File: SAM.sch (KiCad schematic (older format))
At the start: 25 parts

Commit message: ...and now the schematics are in git
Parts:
- removed U?: SAMD21G17A-MU, tm-kicad-lib:QFN-48-1EP-7mm, symbol SAMD21G14A-MU
- added C?: 100nF, tm-kicad-lib:SMD-0402-C, symbol TM_C
- added U?: ATSAMD21J18A-MUT, QFN64, symbol ATSAMD21J18A-MUT
- C?: value 100nF -> 1uF
- J?: value CONN_02X05 DNP -> CONN_02x05, 0.05\"
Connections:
- net labels added: UUT_SWCLK, UUT_SWDIO
- wire segments 144 -> 149
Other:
- moved on the sheet: C?, L?, R?, TP?, X?

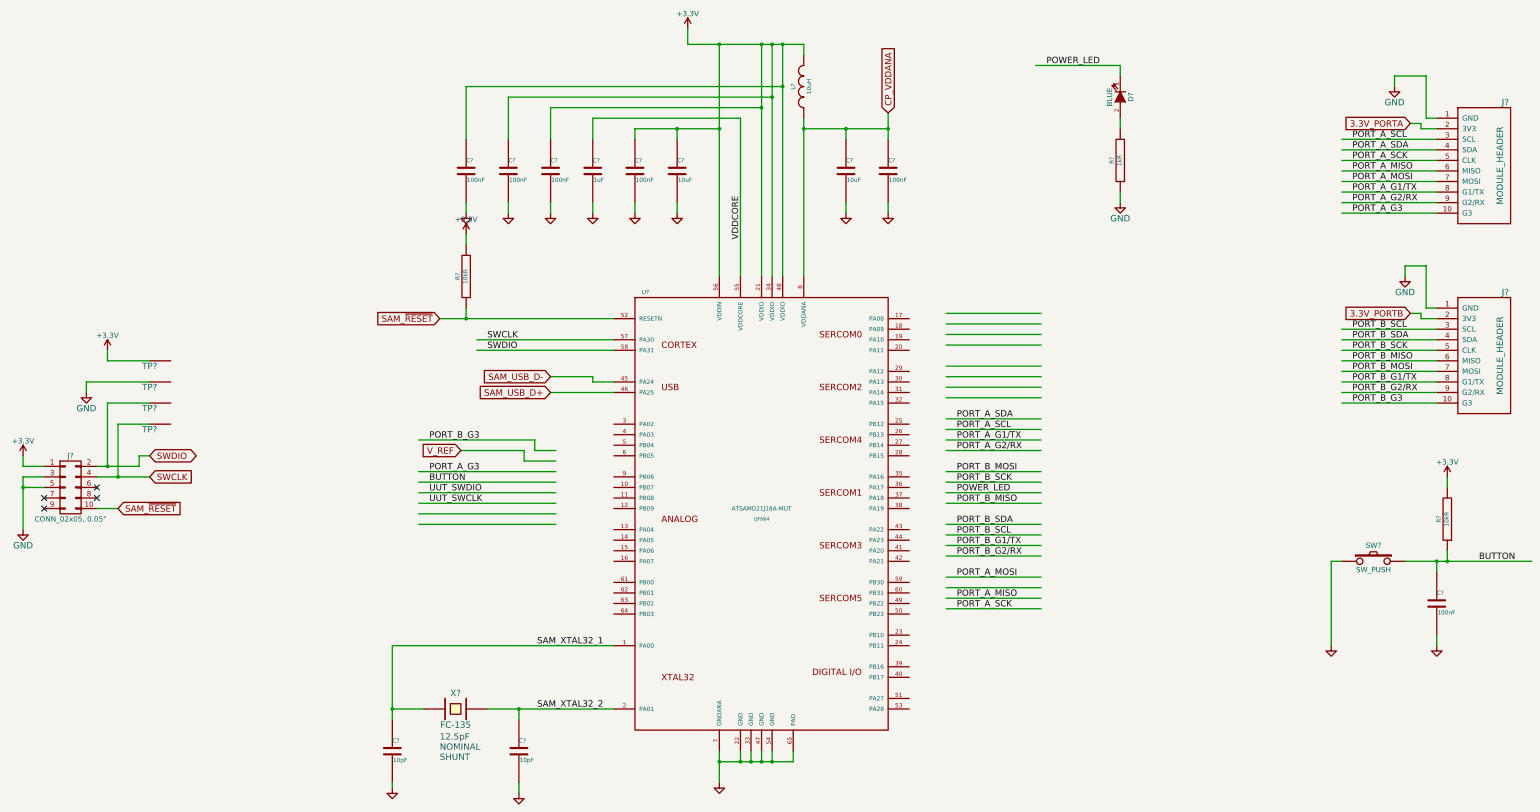
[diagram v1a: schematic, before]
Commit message: sercoms in place
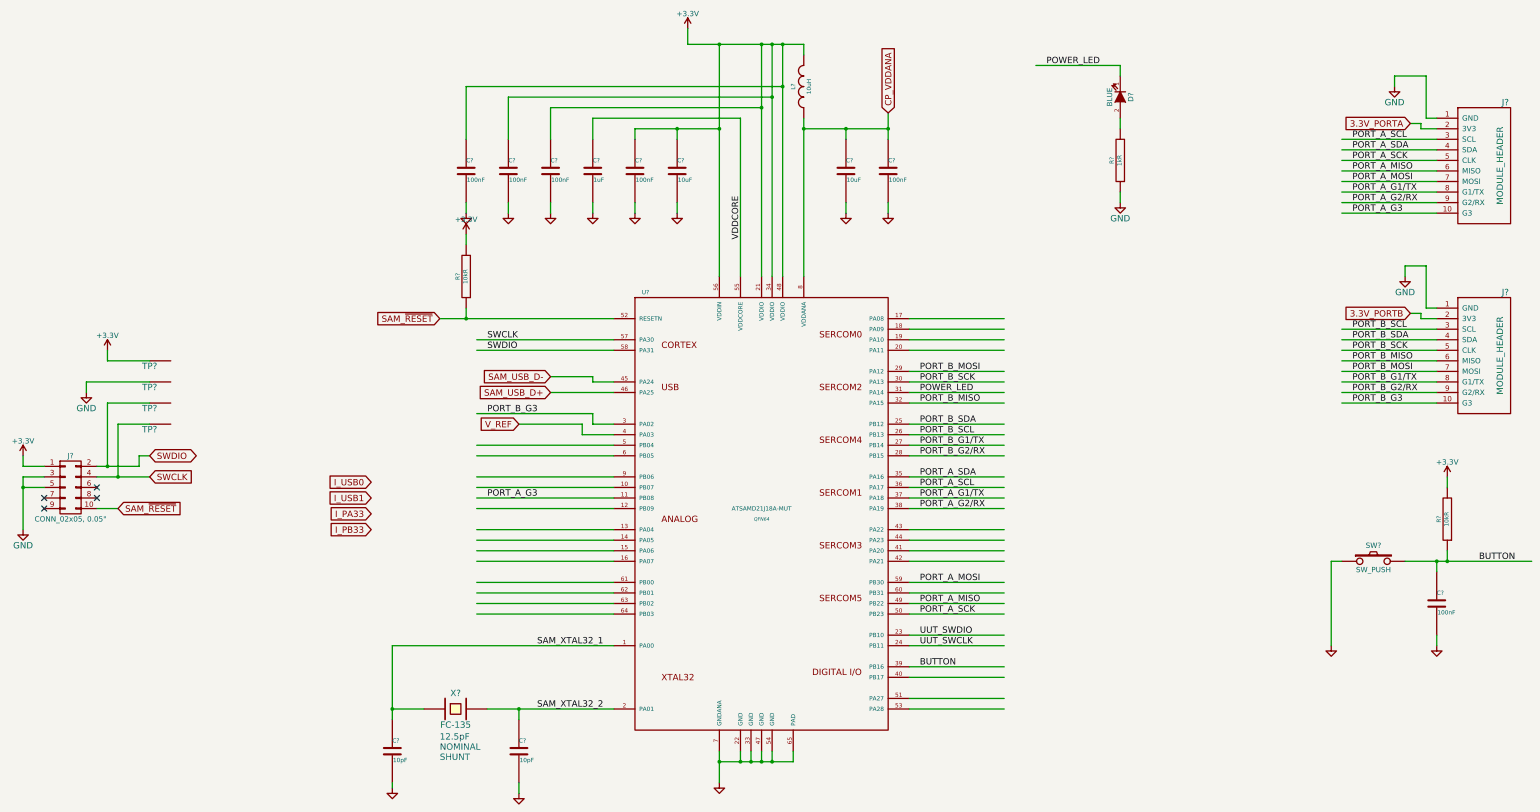
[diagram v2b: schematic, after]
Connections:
- net labels added: I_PA33, I_PB33, I_USB0, I_USB1
- wire segments 149 -> 188
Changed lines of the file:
@@
 Text Label 13800 3600 0    60   ~ 0
 PORT_A_G3
-Text Label 10050 6050 0    60   ~ 0
+Text Label 9700 5100 0    60   ~ 0
 PORT_B_MOSI
-Text Label 10050 6150 0    60   ~ 0
+Text Label 9700 5200 0    60   ~ 0
 PORT_B_SCK
-Text Label 10050 6350 0    60   ~ 0
+Text Label 9700 5400 0    60   ~ 0
 PORT_B_MISO
-Text Label 10050 6550 0    60   ~ 0
+Text Label 9700 5600 0    60   ~ 0
 PORT_B_SDA
-Text Label 10050 6650 0    60   ~ 0
+Text Label 9700 5700 0    60   ~ 0
 PORT_B_SCL
-Text Label 10050 6750 0    60   ~ 0
+Text Label 9700 5800 0    60   ~ 0
 PORT_B_G1/TX
-Text Label 10050 6850 0    60   ~ 0
+Text Label 9700 5900 0    60   ~ 0
 PORT_B_G2/RX
-Text Label 5050 5750 0    60   ~ 0
+Text Label 5600 5500 0    60   ~ 0
 PORT_B_G3
-Text Label 10050 7050 0    60   ~ 0
+Text Label 9700 7100 0    60   ~ 0
 PORT_A_MOSI
-Text Label 10050 7350 0    60   ~ 0
+Text Label 9700 7400 0    60   ~ 0
 PORT_A_SCK
-Text Label 10050 7250 0    60   ~ 0
+Text Label 9700 7300 0    60   ~ 0
 PORT_A_MISO
-Text Label 10050 5550 0    60   ~ 0
+Text Label 9700 6100 0    60   ~ 0
 PORT_A_SDA
-Text Label 10050 5650 0    60   ~ 0
+Text Label 9700 6200 0    60   ~ 0
 PORT_A_SCL
-Text Label 10050 5750 0    60   ~ 0
+Text Label 9700 6300 0    60   ~ 0
 PORT_A_G1/TX
-Text Label 10050 5850 0    60   ~ 0
+Text Label 9700 6400 0    60   ~ 0
 PORT_A_G2/RX
-Text Label 5050 6050 0    60   ~ 0
+Text Label 5600 6300 0    60   ~ 0
 PORT_A_G3
 $Comp
@@
 Text Label 10900 2200 0    60   ~ 0
 POWER_LED
-Text Label 10050 6250 0    60   ~ 0
+Text Label 9700 5300 0    60   ~ 0
 POWER_LED
 Text Notes 5150 8800 0    60   ~ 0
@@
 Text GLabel 14350 4550 0    60   Input ~ 0
 3.3V_PORTB
-Text Label 5050 6150 0    60   ~ 0
+Text Label 9700 7900 0    60   ~ 0
 BUTTON
 Text GLabel 6200 5300 0    60   Input ~ 0
@@
 Text GLabel 6200 5150 0    60   Input ~ 0
 SAM_USB_D-
-Text GLabel 5350 5850 0    60   Input ~ 0
+Text GLabel 5900 5600 0    60   Input ~ 0
 V_REF
-Text Label 5050 6250 0    60   ~ 0
+Text Label 9700 7600 0    60   ~ 0
 UUT_SWDIO
-Text Label 5050 6350 0    60   ~ 0
+Text Label 9700 7700 0    60   ~ 0
 UUT_SWCLK
 $Comp
@@
 	2000 4900 2000 5000
 Wire Wire Line
-	10850 7150 9950 7150
+	10500 7200 9600 7200
 Wire Wire Line
 	1800 5200 1800 5300
@@
 Connection ~ 7800 2000
 Wire Wire Line
-	7800 2000 7800 4200
+	7800 2000 7800 2800
+Wire Wire Line
+	7800 2800 7800 4200
 Connection ~ 8200 2600
 Connection ~ 8200 2000
@@
 Connection ~ 8300 2000
 Wire Wire Line
-	8300 2000 8300 4200
+	8300 2000 8300 2500
+Wire Wire Line
+	8300 2500 8300 4200
 Wire Wire Line
 	7500 2000 7500 1850
@@
 	8200 2600 6200 2600
 Wire Wire Line
-	8200 2000 8200 4200
+	8200 2000 8200 2600
+Wire Wire Line
+	8200 2600 8200 4200
 Wire Wire Line
 	8000 2700 8000 4200
@@
 	7000 2800 7000 2900
 Wire Wire Line
-	7000 2800 7800 2800
+	7000 2800 7400 2800
+Wire Wire Line
+	7400 2800 7800 2800
 Connection ~ 8600 2800
 Connection ~ 9000 2800
 Wire Wire Line
-	9400 2650 9400 2900
+	9400 2650 9400 2800
+Wire Wire Line
+	9400 2800 9400 2900
 Wire Wire Line
 	9000 2800 9000 2900
 Wire Wire Line
-	8600 2800 9400 2800
-Wire Wire Line
-	8600 2700 8600 4200
+	8600 2800 9000 2800
+Wire Wire Line
+	9000 2800 9400 2800
+Wire Wire Line
+	8600 2700 8600 2800
+Wire Wire Line
+	8600 2800 8600 4200
 Wire Wire Line
 	4700 9000 4700 9050
@@
 	4700 8300 5000 8300
 Wire Wire Line
-	4700 7700 4700 8400
-Wire Wire Line
-	9950 7050 10850 7050
-Wire Wire Line
-	9950 7250 10850 7250
-Wire Wire Line
-	9950 7350 10850 7350
-Wire Wire Line
-	9950 4850 10850 4850
-Wire Wire Line
-	9950 4750 10850 4750
-Wire Wire Line
-	9950 4650 10850 4650
-Wire Wire Line
-	10850 4550 9950 4550
-Wire Wire Line
-	9950 5850 10850 5850
-Wire Wire Line
-	9950 5750 10850 5750
-Wire Wire Line
-	9950 5650 10850 5650
-Wire Wire Line
-	9950 5550 10850 5550
-Wire Wire Line
-	9950 6850 10850 6850
-Wire Wire Line
-	9950 6750 10850 6750
-Wire Wire Line
-	9950 6650 10850 6650
-Wire Wire Line
-	9950 6550 10850 6550
-Wire Wire Line
-	9950 6350 10850 6350
-Wire Wire Line
-	9950 6150 10850 6150
-Wire Wire Line
-	9950 6050 10850 6050
-Wire Wire Line
-	5600 8300 6800 8300
+	4700 7700 4700 8300
+Wire Wire Line
+	4700 8300 4700 8400
+Wire Wire Line
+	9600 7100 10500 7100
+Wire Wire Line
+	9600 7300 10500 7300
+Wire Wire Line
+	9600 7400 10500 7400
+Wire Wire Line
+	9600 4900 10500 4900
+Wire Wire Line
+	9600 4800 10500 4800
+Wire Wire Line
+	9600 4700 10500 4700
+Wire Wire Line
+	10500 4600 9600 4600
+Wire Wire Line
+	9600 6400 10500 6400
+Wire Wire Line
+	9600 6300 10500 6300
+Wire Wire Line
+	9600 6200 10500 6200
+Wire Wire Line
+	9600 6100 10500 6100
+Wire Wire Line
+	9600 5900 10500 5900
+Wire Wire Line
+	9600 5800 10500 5800
+Wire Wire Line
+	9600 5700 10500 5700
+Wire Wire Line
+	9600 5600 10500 5600
+Wire Wire Line
+	9600 5400 10500 5400
+Wire Wire Line
+	9600 5200 10500 5200
+Wire Wire Line
+	9600 5100 10500 5100
+Wire Wire Line
+	5600 8300 5900 8300
+Wire Wire Line
+	5900 8300 6800 8300
 Wire Wire Line
 	4700 7700 6800 7700
 Wire Wire Line
-	6250 6050 4950 6050
-Wire Wire Line
-	6250 6150 4950 6150
+	9600 7900 10500 7900
 Wire Wire Line
 	6800 5200 6600 5200
@@
 	6800 4800 5500 4800
 Wire Wire Line
-	5150 4600 6800 4600
-Wire Wire Line
-	7500 2000 8600 2000
+	5150 4600 5400 4600
+Wire Wire Line
+	5400 4600 6800 4600
+Wire Wire Line
+	7500 2000 7800 2000
+Wire Wire Line
+	7800 2000 8200 2000
+Wire Wire Line
+	8200 2000 8300 2000
+Wire Wire Line
+	8300 2000 8400 2000
+Wire Wire Line
+	8400 2000 8600 2000
 Wire Wire Line
 	7400 2900 7400 2800
 Connection ~ 7400 2800
 Wire Wire Line
-	7800 8700 7800 9000
-Wire Wire Line
-	7800 8800 8500 8800
+	7800 8700 7800 8800
+Wire Wire Line
+	7800 8800 7800 9000
+Wire Wire Line
+	7800 8800 8000 8800
+Wire Wire Line
+	8000 8800 8100 8800
+Wire Wire Line
+	8100 8800 8200 8800
+Wire Wire Line
+	8200 8800 8300 8800
+Wire Wire Line
+	8300 8800 8500 8800
 Wire Wire Line
 	8000 8800 8000 8700
@@
 Connection ~ 8200 8800
 Wire Wire Line
-	9950 5050 10850 5050
-Wire Wire Line
-	9950 5150 10850 5150
-Wire Wire Line
-	9950 5250 10850 5250
-Wire Wire Line
-	10850 5350 9950 5350
-Wire Wire Line
-	4950 6250 6250 6250
+	9600 6600 10500 6600
+Wire Wire Line
+	9600 6700 10500 6700
+Wire Wire Line
+	9600 6800 10500 6800
+Wire Wire Line
+	10500 6900 9600 6900
+Wire Wire Line
+	10500 7600 9600 7600
 Wire Wire Line
 	5400 3800 5400 3900
 Connection ~ 9400 2800
 Wire Wire Line
-	9950 6250 10850 6250
+	9600 5300 10500 5300
 Wire Wire Line
 	14600 7600 14600 7700
@@
 	14700 6100 14700 6200
 Wire Wire Line
-	14300 6900 15500 6900
+	14300 6900 14600 6900
+Wire Wire Line
+	14600 6900 14700 6900
+Wire Wire Line
+	14700 6900 15500 6900
 Wire Wire Line
 	14700 6900 14700 6800
@@
 	1400 6200 1200 6200
 Wire Wire Line
-	1200 6100 1200 6600
+	1200 6100 1200 6200
+Wire Wire Line
+	1200 6200 1200 6600
 Wire Wire Line
 	1400 6100 1200 6100
@@
 	2100 6400 1900 6400
 Wire Wire Line
-	1900 6100 2400 6100
-Wire Wire Line
-	1900 6000 2300 6000
+	1900 6100 2100 6100
+Wire Wire Line
+	2100 6100 2400 6100
+Wire Wire Line
+	1900 6000 2000 6000
+Wire Wire Line
+	2000 6000 2300 6000
 Wire Wire Line
 	1200 6000 1200 5900
@@
 	14200 2300 14200 2400
 Wire Wire Line
-	4950 6550 6250 6550
-Wire Wire Line
-	4950 6450 6250 6450
-Wire Wire Line
-	4950 6350 6250 6350
+	10500 8300 9600 8300
+Wire Wire Line
+	10500 8200 9600 8200
+Wire Wire Line
+	10500 7700 9600 7700
 Wire Wire Line
 	11600 2300 11600 2200
@@
 	11600 2200 10800 2200
 Wire Wire Line
-	4950 5750 6050 5750
-Wire Wire Line
-	6050 5750 6050 5850
-Wire Wire Line
-	6050 5850 6250 5850
-Wire Wire Line
-	6250 5950 5950 5950
-Wire Wire Line
-	5950 5950 5950 5850
-Wire Wire Line
-	5950 5850 5350 5850
+	5500 5500 6600 5500
+Wire Wire Line
+	6600 5500 6600 5600
+Wire Wire Line
+	6600 5600 6800 5600
+Wire Wire Line
+	6800 5700 6500 5700
+Wire Wire Line
+	6500 5700 6500 5600
+Wire Wire Line
+	6500 5600 5900 5600
 Wire Wire Line
 	5400 3600 5400 3500
@@
 	5400 2400 8400 2400
 Wire Wire Line
-	8400 2000 8400 4200
+	8400 2000 8400 2400
+Wire Wire Line
+	8400 2400 8400 4200
 Connection ~ 8400 2000
 Connection ~ 8400 2400
@@
 	8500 8800 8500 8700
 Connection ~ 8300 8800
+Wire Wire Line
+	6800 5800 5500 5800
+Wire Wire Line
+	6800 5900 5500 5900
+Wire Wire Line
+	6800 6100 5500 6100
+Wire Wire Line
+	6800 6200 5500 6200
+Wire Wire Line
+	6800 6300 5500 6300
+Wire Wire Line
+	6800 6400 5500 6400
+Wire Wire Line
+	6800 6600 5500 6600
+Wire Wire Line
+	6800 6700 5500 6700
+Wire Wire Line
+	6800 6800 5500 6800
+Wire Wire Line
+	6800 6900 5500 6900
+Wire Wire Line
+	6800 7100 5500 7100
+Wire Wire Line
+	6800 7200 5500 7200
+Wire Wire Line
+	6800 7300 5500 7300
+Wire Wire Line
+	6800 7400 5500 7400
+Text GLabel 4500 6150 0    60   Input ~ 0
+I_USB0
+Text GLabel 4500 6300 0    60   Input ~ 0
+I_USB1
+Text GLabel 4500 6450 0    60   Input ~ 0
+I_PA33
+Text GLabel 4500 6600 0    60   Input ~ 0
+I_PB33
+Wire Wire Line
+	10500 8000 9600 8000
 $EndSCHEMATC
